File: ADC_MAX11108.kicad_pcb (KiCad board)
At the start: 4 copper layers, 100 x 100 mm, 326 parts, among them IC1 MAX11108AVB+T, IC10 MAX11108AVB+T, IC11 MAX11108AVB+T, IC12 MAX11108AVB+T, IC13 MAX11108AVB+T, IC14 MAX11108AVB+T, IC15 MAX11108AVB+T, IC16 MAX11108AVB+T, IC17 MAX11108AVB+T, IC18 MAX11108AVB+T, IC19 MAX11108AVB+T, IC2 MAX11108AVB+T, IC20 MAX11108AVB+T, IC21 MAX11108AVB+T, IC22 524SDCGI8, IC23 MAX11108AVB+T, IC24 524SDCGI8, IC25 MAX11108AVB+T, IC26 524SDCGI8, IC27 MAX11108AVB+T, IC28 524SDCGI8, IC29 MAX11108AVB+T, IC3 MAX11108AVB+T, IC30 LMS1587CS-ADJ, IC31 LMS1587CS-3.3, IC4 MAX11108AVB+T, IC5 MAX11108AVB+T, IC6 MAX11108AVB+T, IC7 MAX11108AVB+T, IC8 MAX11108AVB+T, IC9 MAX11108AVB+T, J1 Conn_01x02_Pin, J10 Conn_01x02_Pin, J11 Conn_01x02_Pin, J2 Conn_01x02_Pin, J3 Conn_01x07_Pin, J4 Conn_01x07_Pin, J5 Conn_01x07_Pin, J6 Conn_01x08_Pin, J7 Conn_01x08_Pin, J8 Conn_01x02_Pin, J9 Conn_01x02_Pin

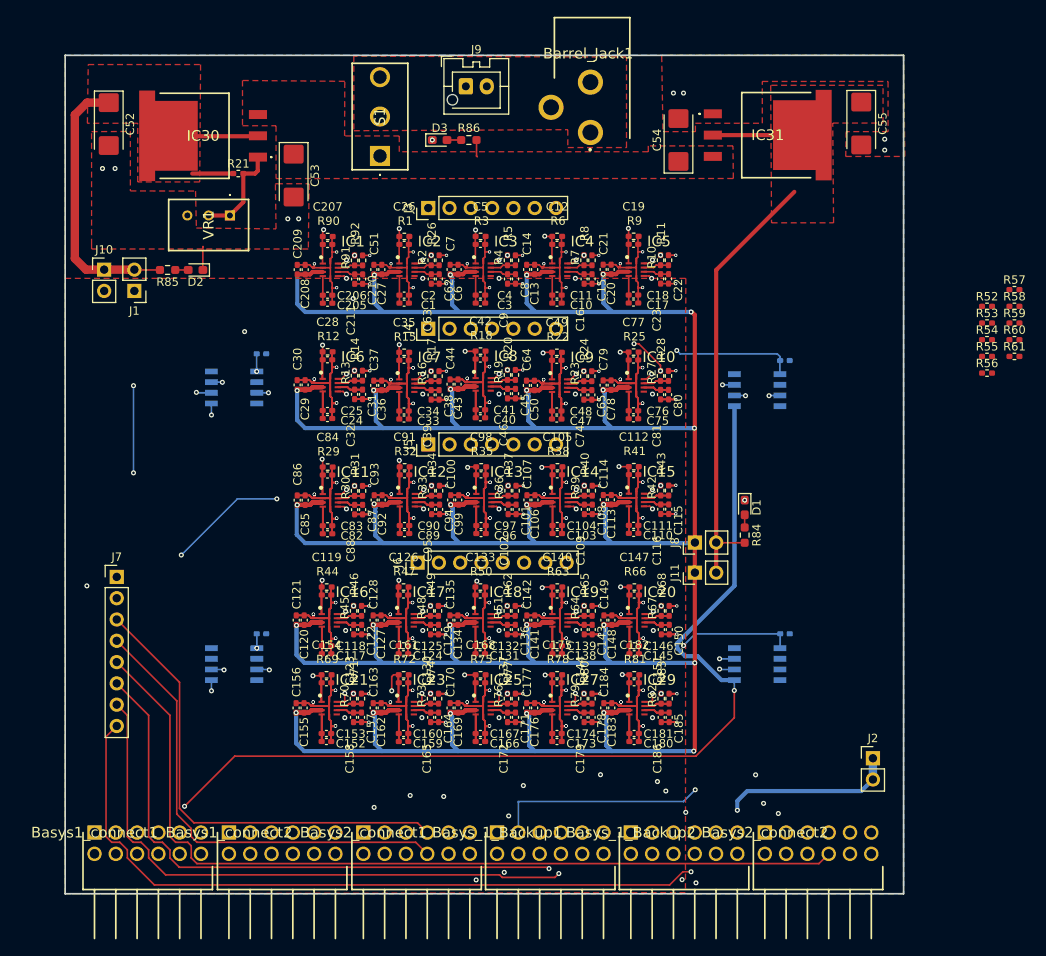
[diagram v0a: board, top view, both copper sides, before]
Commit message: fixed Vadj plane, cleaned up connections
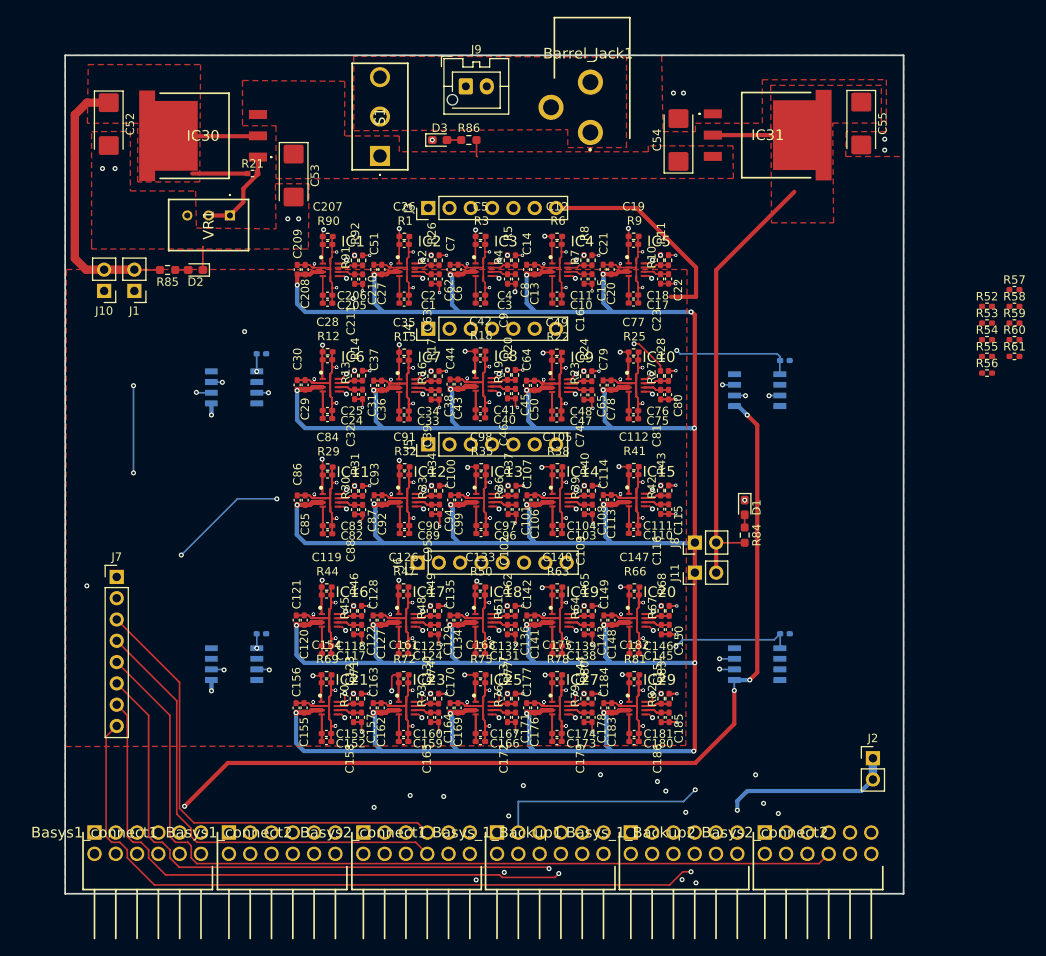
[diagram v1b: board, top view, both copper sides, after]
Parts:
- moved J10 2.54 mm to (104.5, 77.0), turned to 180 degrees
- moved R21 1.70 mm to (122.2, 63.0)
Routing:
- net 3.3_ADJ: track 316.1 -> 343.2 mm
- net GND: track 764.1 -> 756.2 mm
- net CS_4: track 69.9 -> 76.0 mm
- net CS_5: track 83.7 -> 89.3 mm
- net CS_2: track 90.4 -> 94.9 mm
- net Serial_CLK: track 119.0 -> 115.6 mm, vias 2 -> 4
- net CS_1: track 86.8 -> 90.0 mm
- net Net-(IC30-OUTPUT): track 47.1 -> 48.8 mm
- net Net-(IC30-ADJ/GND): track 11.6 -> 10.8 mm
- net 3.3VRef: vias 28 -> 29
- net /Dout10: vias 5 -> 4
